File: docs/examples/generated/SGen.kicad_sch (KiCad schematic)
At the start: 23 parts, among them Q1 2N3904, Q2 2N3904

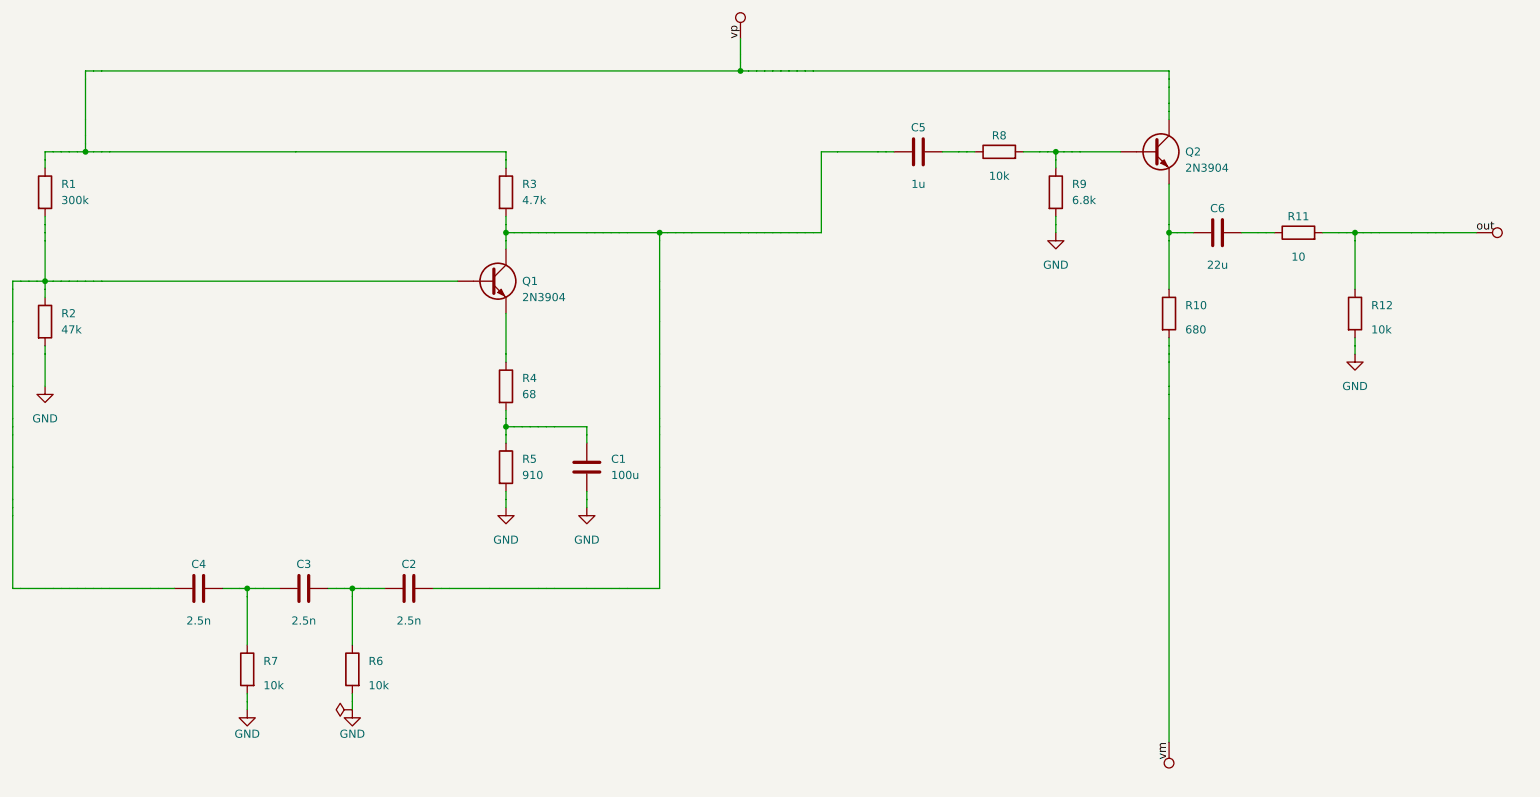
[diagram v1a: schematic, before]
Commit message: Port fbcode test fixtures and compatibility fixes
Sync the portable D127189972 fixes into circuitsense-gen-pyre: symbol fixtures for hosts without KiCad, explicit integration markers, packaged-model path handling, formatting, and refreshed sine-generator schematics. Preserve the branch enhancements and document unit and integration testing.

Validation: 115 tests passed with KiCad/ngspice; 94 unit tests passed without KiCad.
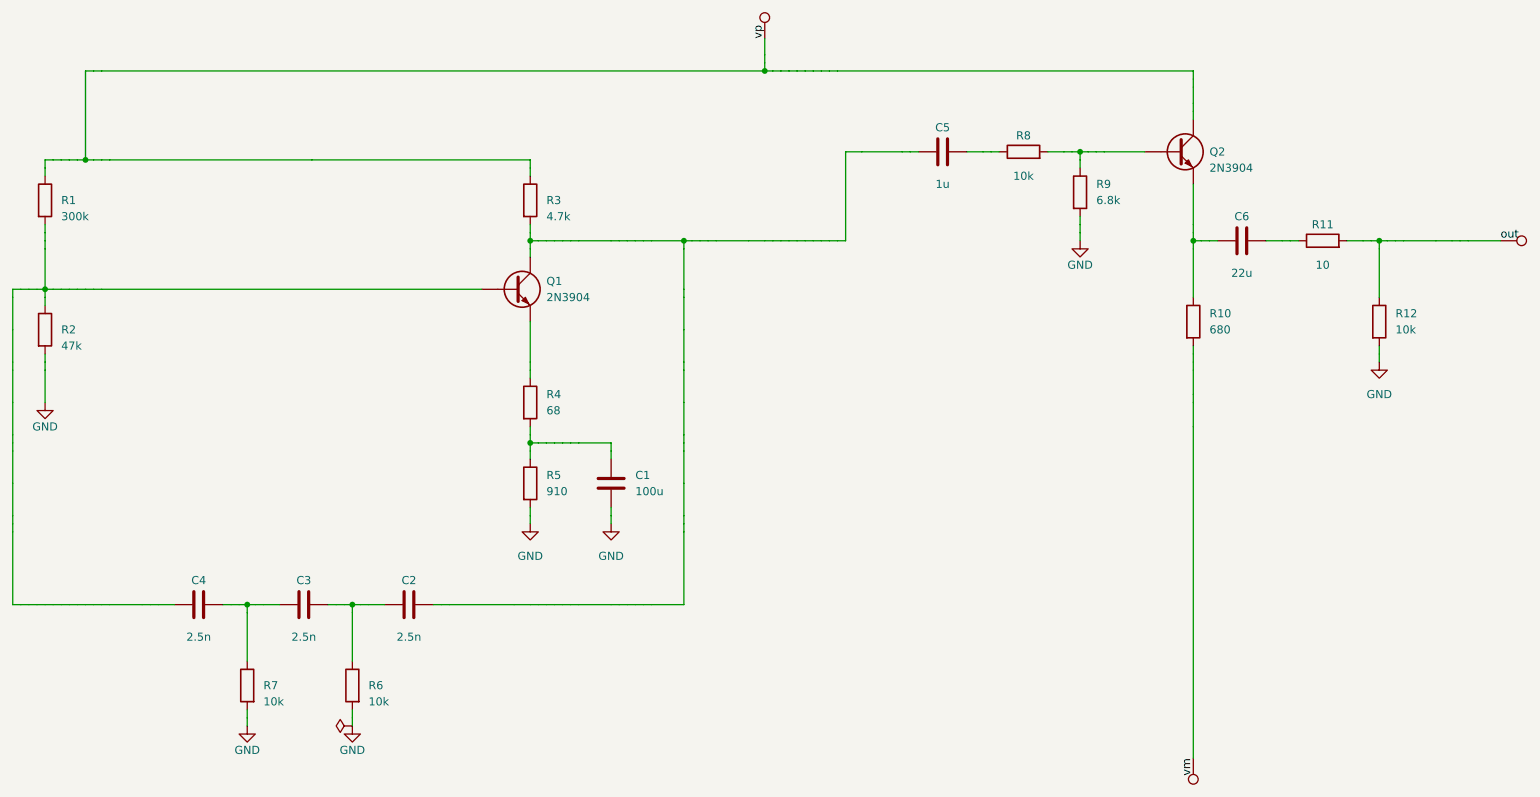
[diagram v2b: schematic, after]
